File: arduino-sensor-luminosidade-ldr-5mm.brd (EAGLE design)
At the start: 68.6 x 53.3 mm, 5 parts

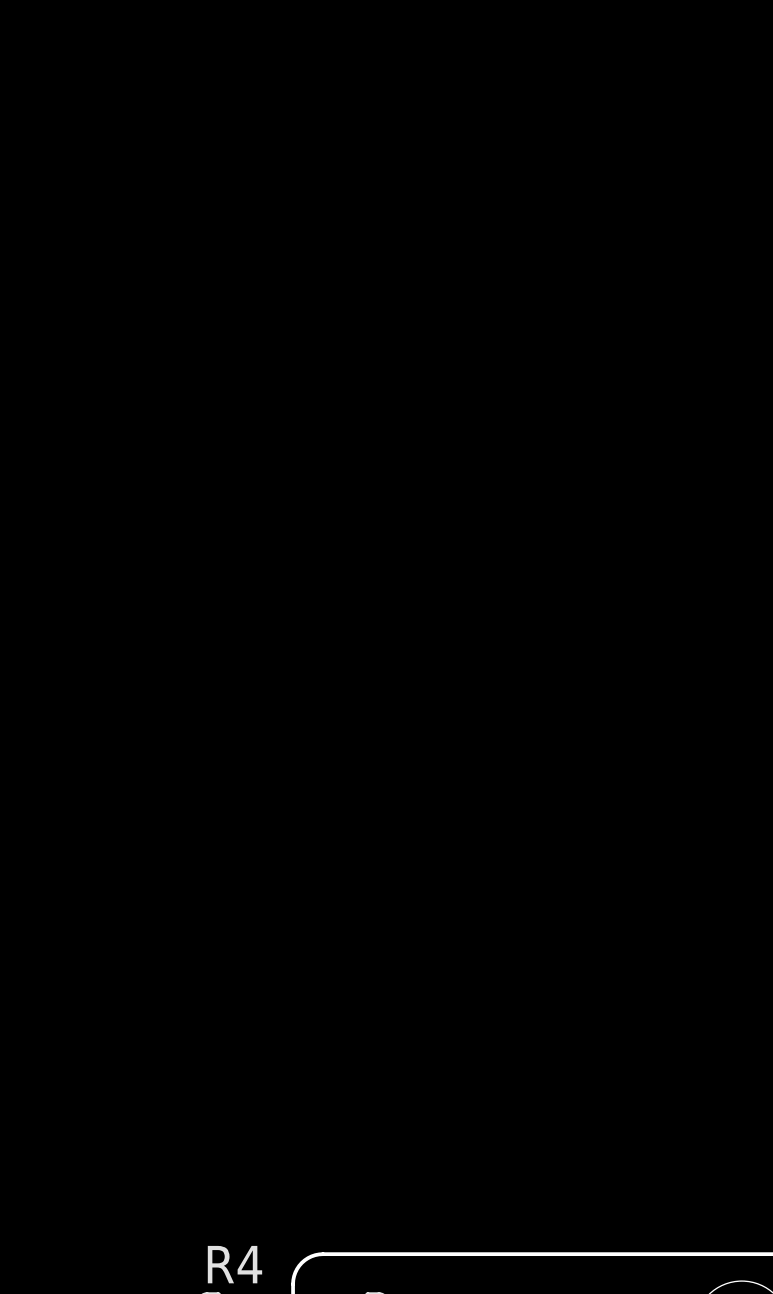
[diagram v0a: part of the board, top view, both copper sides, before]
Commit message: Add Relé SPDT ao projeto
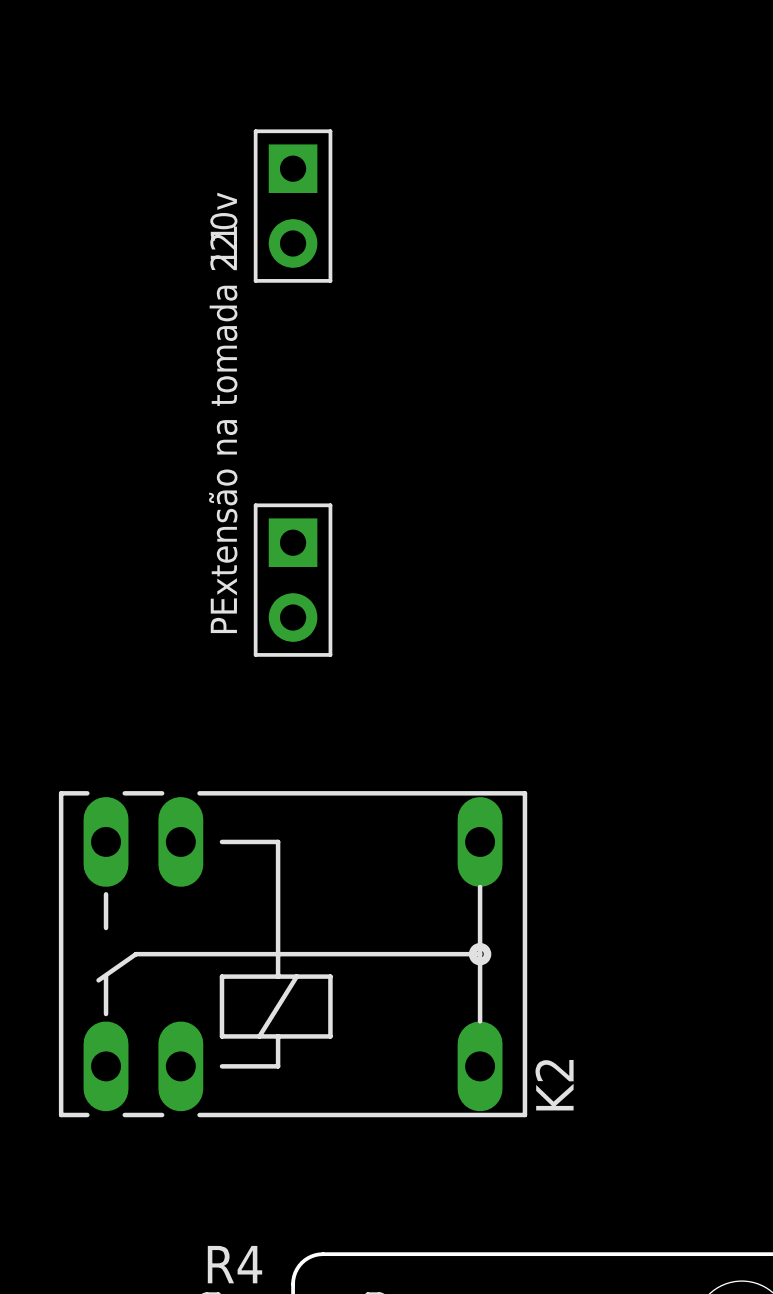
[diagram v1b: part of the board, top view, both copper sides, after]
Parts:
- added K2: (no value), AUTODESK_CIRCUITS_BREADBOARD:M3XXH
- added L1: (no value), AUTODESK_CIRCUITS_BREADBOARD:2P-2.54-65/35MIL
- added PExtensão na tomada 220v: 5V, AUTODESK_CIRCUITS_BREADBOARD:2P-2.54-65/35MIL
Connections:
- new net N$5: L1.1, PExtensão na tomada 220v.2
- new net N$6: K2.O, L1.2
- new net N$7: K2.P, PExtensão na tomada 220v.1
- new net N$8: K2.2, U1.GND..
- new net N$9: K2.1, U1.10
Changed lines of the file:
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@@
 </autorouter>
 <elements>
-<element value="" name="U1" library="AUTODESK_CIRCUITS_BREADBOARD" package="ARDUINO_UNO" x="5" y="10.08"></element><element value="" name="R1" library="AUTODESK_CIRCUITS_BREADBOARD" package="PHOTORESISTOR-2.54" x="5" y="22.78"></element><element value="10k‎Ω" name="R3" library="AUTODESK_CIRCUITS_BREADBOARD" package="0207/10" x="5" y="35.480000000000004"></element><element value="" name="D1" library="AUTODESK_CIRCUITS_BREADBOARD" package="LED5MM" x="5" y="48.18"></element><element value="300‎Ω" name="R4" library="AUTODESK_CIRCUITS_BREADBOARD" package="0207/10" x="5" y="60.879999999999995"></element></elements>
+<element value="" name="U1" library="AUTODESK_CIRCUITS_BREADBOARD" package="ARDUINO_UNO" x="5" y="10.08"></element><element value="" name="R1" library="AUTODESK_CIRCUITS_BREADBOARD" package="PHOTORESISTOR-2.54" x="5" y="22.78"></element><element value="10k‎Ω" name="R3" library="AUTODESK_CIRCUITS_BREADBOARD" package="0207/10" x="5" y="35.480000000000004"></element><element value="" name="D1" library="AUTODESK_CIRCUITS_BREADBOARD" package="LED5MM" x="5" y="48.18"></element><element value="300‎Ω" name="R4" library="AUTODESK_CIRCUITS_BREADBOARD" package="0207/10" x="5" y="60.879999999999995"></element><element value="" name="K2" library="AUTODESK_CIRCUITS_BREADBOARD" package="M3XXH" x="5" y="73.58"></element><element value="5V" name="PExtensão na tomada 220v" library="AUTODESK_CIRCUITS_BREADBOARD" package="2P-2.54-65/35MIL" x="5" y="86.28"></element><element value="" name="L1" library="AUTODESK_CIRCUITS_BREADBOARD" package="2P-2.54-65/35MIL" x="5" y="98.98"></element></elements>
 <signals>
-<signal name="N$1"><contactref element="D1" pad="A"></contactref><contactref element="U1" pad="2"></contactref><wire x1="3.73" y1="48.18" x2="63.42" y2="60.879999999999995" width="0" layer="19" extent="1-1"></wire></signal><signal name="N$2"><contactref element="R3" pad="1"></contactref><contactref element="U1" pad="5V"></contactref><wire x1="-0.08000000000000007" y1="35.480000000000004" x2="43.1" y2="12.620000000000001" width="0" layer="19" extent="1-1"></wire></signal><signal name="N$3"><contactref element="R1" pad="P$2"></contactref><contactref element="U1" pad="A0"></contactref><wire x1="6.27" y1="22.78" x2="55.8" y2="12.620000000000001" width="0" layer="19" extent="1-1"></wire><contactref element="R3" pad="2"></contactref><wire x1="55.8" y1="12.620000000000001" x2="10.08" y2="35.480000000000004" width="0" layer="19" extent="1-1"></wire></signal><signal name="N$4"><contactref element="R4" pad="1"></contactref><contactref element="D1" pad="K"></contactref><wire x1="-0.08000000000000007" y1="60.879999999999995" x2="6.27" y2="48.18" width="0" layer="19" extent="1-1"></wire><contactref element="R4" pad="2"></contactref><wire x1="6.27" y1="48.18" x2="10.08" y2="60.879999999999995" width="0" layer="19" extent="1-1"></wire><contactref element="R1" pad="P$1"></contactref><wire x1="10.08" y1="60.879999999999995" x2="3.73" y2="22.78" width="0" layer="19" extent="1-1"></wire><contactref element="U1" pad="GND."></contactref><wire x1="3.73" y1="22.78" x2="48.18" y2="12.620000000000001" width="0" layer="19" extent="1-1"></wire></signal></signals>
+<signal name="N$1"><contactref element="D1" pad="A"></contactref><contactref element="U1" pad="2"></contactref><wire x1="3.73" y1="48.18" x2="63.42" y2="60.879999999999995" width="0" layer="19" extent="1-1"></wire></signal><signal name="N$2"><contactref element="R3" pad="1"></contactref><contactref element="U1" pad="5V"></contactref><wire x1="-0.08000000000000007" y1="35.480000000000004" x2="43.1" y2="12.620000000000001" width="0" layer="19" extent="1-1"></wire></signal><signal name="N$3"><contactref element="R1" pad="P$2"></contactref><contactref element="U1" pad="A0"></contactref><wire x1="6.27" y1="22.78" x2="55.8" y2="12.620000000000001" width="0" layer="19" extent="1-1"></wire><contactref element="R3" pad="2"></contactref><wire x1="55.8" y1="12.620000000000001" x2="10.08" y2="35.480000000000004" width="0" layer="19" extent="1-1"></wire></signal><signal name="N$4"><contactref element="R4" pad="1"></contactref><contactref element="D1" pad="K"></contactref><wire x1="-0.08000000000000007" y1="60.879999999999995" x2="6.27" y2="48.18" width="0" layer="19" extent="1-1"></wire><contactref element="R4" pad="2"></contactref><wire x1="6.27" y1="48.18" x2="10.08" y2="60.879999999999995" width="0" layer="19" extent="1-1"></wire><contactref element="R1" pad="P$1"></contactref><wire x1="10.08" y1="60.879999999999995" x2="3.73" y2="22.78" width="0" layer="19" extent="1-1"></wire><contactref element="U1" pad="GND."></contactref><wire x1="3.73" y1="22.78" x2="48.18" y2="12.620000000000001" width="0" layer="19" extent="1-1"></wire></signal><signal name="N$5"><contactref element="L1" pad="1"></contactref><contactref element="PExtensão na tomada 220v" pad="2"></contactref><wire x1="5" y1="100.25" x2="5" y2="85.01" width="0" layer="19" extent="1-1"></wire></signal><signal name="N$6"><contactref element="L1" pad="2"></contactref><contactref element="K2" pad="O"></contactref><wire x1="5" y1="97.71000000000001" x2="-1.3499999999999996" y2="69.77" width="0" layer="19" extent="1-1"></wire></signal><signal name="N$7"><contactref element="K2" pad="P"></contactref><contactref element="PExtensão na tomada 220v" pad="1"></contactref><wire x1="11.35" y1="69.77" x2="5" y2="87.55" width="0" layer="19" extent="1-1"></wire></signal><signal name="N$8"><contactref element="K2" pad="2"></contactref><contactref element="U1" pad="GND.."></contactref><wire x1="1.19" y1="69.77" x2="45.64" y2="12.620000000000001" width="0" layer="19" extent="1-1"></wire></signal><signal name="N$9"><contactref element="K2" pad="1"></contactref><contactref element="U1" pad="10"></contactref><wire x1="1.19" y1="77.39" x2="41.576" y2="60.879999999999995" width="0" layer="19" extent="1-1"></wire></signal></signals>
 </board>
 </drawing>
